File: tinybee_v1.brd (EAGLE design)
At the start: 47.6 x 27.8 mm, 22 parts, among them U1 ATTINY85-20S

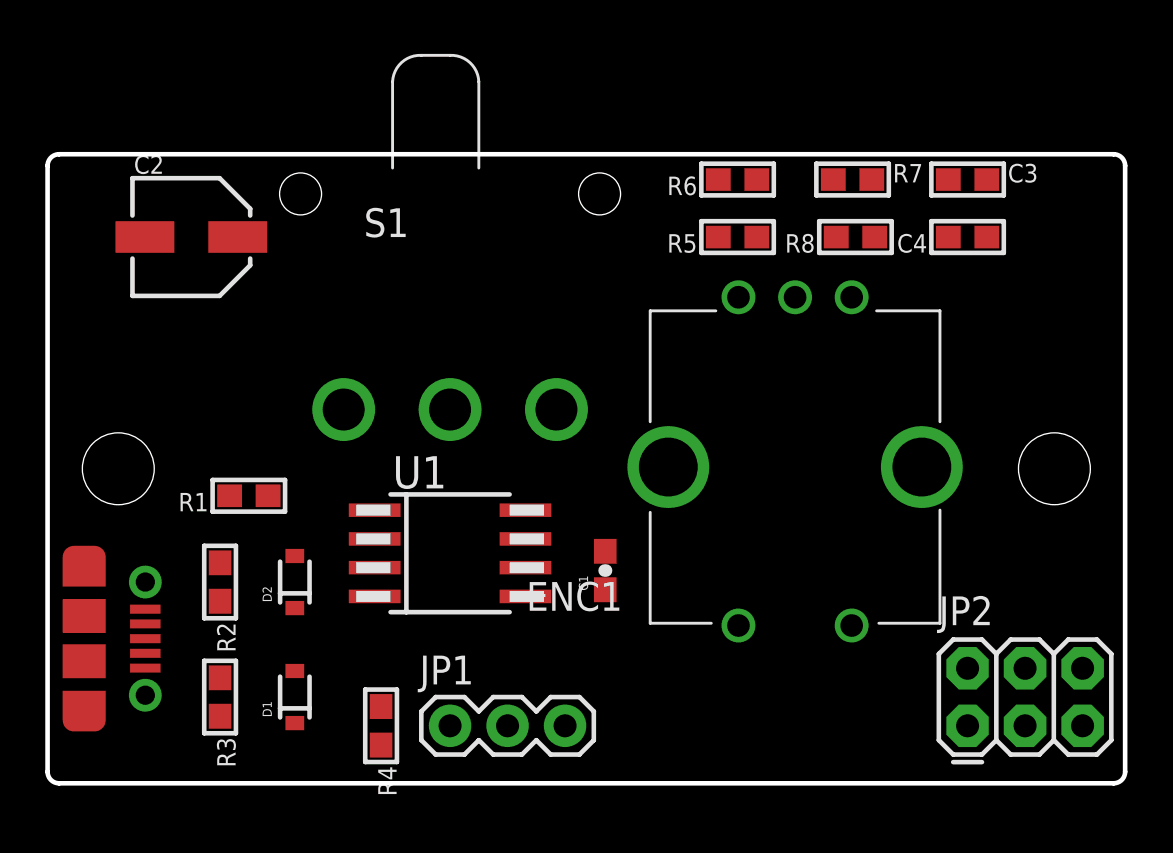
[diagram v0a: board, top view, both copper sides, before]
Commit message: Fixes after Eran review
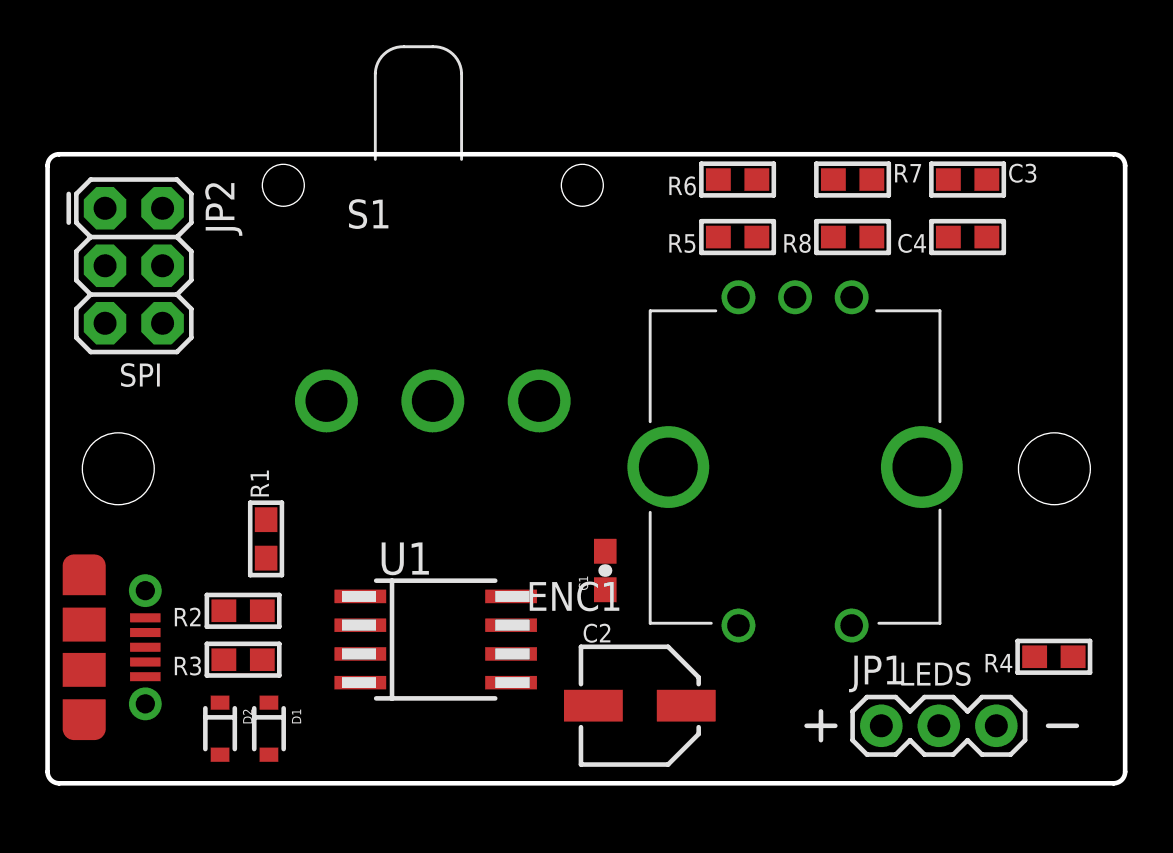
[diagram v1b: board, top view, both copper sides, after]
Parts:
- moved JP2 44.4 mm to (2.54, 25.4), turned to 270 degrees
- moved R4 29.9 mm to (44.5, 5.59), turned to 180 degrees
- moved C2 28.7 mm to (26.2, 3.43)
- moved JP1 19.0 mm to (36.8, 2.54)
- moved D2 7.27 mm to (7.62, 2.41), turned to 270 degrees
- moved U1 3.86 mm to (17.1, 6.35)
- moved R1 2.05 mm to (9.65, 10.8), turned to 90 degrees
- moved R3 1.94 mm to (8.64, 5.46), turned to 180 degrees
- moved D1 1.81 mm to (9.78, 2.41), turned to 270 degrees
- moved R2 1.63 mm to (8.64, 7.62), turned to 180 degrees
- moved S1 0.85 mm to (17.0, 16.9)
- moved USB 0.38 mm to (4.32, 8.51)
- moved R8 0.13 mm to (35.6, 24.1)
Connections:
- net N$1 renamed VBUS
- removed net N$5: C1.1, U1.8
- net GND: now also C1.2
- net VCC: now also C1.1, U1.8; no longer C1.2
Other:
- board text added: "LEDS"
- board text added: "SPI"

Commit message: moved a few pieces
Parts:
- moved ENC1 1.27 mm to (34.3, 14.0)
- moved C2 0.65 mm to (25.5, 3.56)
- moved C3 0.25 mm to (40.6, 26.4), turned to 180 degrees
- moved R6 0.25 mm to (30.5, 26.4)
- moved R7 0.25 mm to (35.6, 26.4)
- turned R8 to 0 degrees
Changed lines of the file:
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@@
 <attribute name="PROD_ID" value="CAP-00810" x="24.638" y="9.398" size="1.778" layer="27" rot="R90" display="off"/>
 </element>
-<element name="C2" library="microbuilder" package="PANASONIC_C" value="47uF" x="26.162" y="3.429"/>
-<element name="C3" library="microbuilder" package="0603" value="0.1uF" x="40.64" y="26.67"/>
+<element name="C2" library="microbuilder" package="PANASONIC_C" value="47uF" x="25.527" y="3.556"/>
+<element name="C3" library="microbuilder" package="0603" value="0.1uF" x="40.64" y="26.416" rot="R180"/>
 <element name="C4" library="microbuilder" package="0603" value="0.1uF" x="40.64" y="24.13" rot="R180"/>
 <element name="D1" library="SparkFun-DiscreteSemi" package="SOD-323" value="3.6V" x="9.779" y="2.413" rot="R270">
@@
 <element name="JP1" library="SparkFun-Connectors" package="1X03" value="LEDS" x="36.83" y="2.54"/>
 <element name="R5" library="microbuilder" package="0603" value="10k" x="30.48" y="24.13" rot="R180"/>
-<element name="R6" library="microbuilder" package="0603" value="10k" x="30.48" y="26.67" rot="R180"/>
-<element name="R7" library="microbuilder" package="0603" value="10k" x="35.56" y="26.67"/>
-<element name="R8" library="microbuilder" package="0603" value="10k" x="35.56" y="24.13" rot="R180"/>
+<element name="R6" library="microbuilder" package="0603" value="10k" x="30.48" y="26.416" rot="R180"/>
+<element name="R7" library="microbuilder" package="0603" value="10k" x="35.56" y="26.416"/>
+<element name="R8" library="microbuilder" package="0603" value="10k" x="35.56" y="24.13"/>
 <element name="U1" library="_hhn_attiny25_45_85" package="SOIC8_EIAJ_208MIL" value="ATTINY85-20S" x="17.145" y="6.35" rot="R270"/>
 <element name="USB" library="GeekAmmo" package="USB-MICRO-MOLEX-105017-0001" value="USB-CON-5PIN-105017-0001" x="4.318" y="8.509" rot="R270"/>
@@
 <element name="R2" library="microbuilder" package="0603" value="68R" x="8.636" y="7.62" rot="R180"/>
 <element name="R4" library="microbuilder" package="0603" value="220R" x="44.45" y="5.588" rot="R180"/>
-<element name="ENC1" library="Custom" package="ROTARY-ENCODER-PEC12R" value="" x="33.02" y="13.97" rot="R180"/>
+<element name="ENC1" library="Custom" package="ROTARY-ENCODER-PEC12R" value="" x="34.29" y="13.97" rot="R180"/>
 <element name="U$1" library="Custom" package="FB-30" value="" x="0" y="0"/>
 <element name="S1" library="Custom" package="SWITCH-SPDT-RIGHTANGLE-500" value="" x="17.018" y="16.891"/>
@@
 <contactref element="U1" pad="8"/>
 <contactref element="C1" pad="1"/>
-<wire x1="34.71" y1="24.13" x2="36.41" y2="26.67" width="0" layer="19" extent="1-1"/>
-<wire x1="24.638" y1="8.548" x2="34.71" y2="24.13" width="0" layer="19" extent="1-1"/>
+<wire x1="36.41" y1="24.13" x2="36.41" y2="26.416" width="0" layer="19" extent="1-1"/>
+<wire x1="24.638" y1="8.548" x2="36.41" y2="24.13" width="0" layer="19" extent="1-1"/>
 <wire x1="20.475" y1="8.255" x2="24.638" y2="8.548" width="0" layer="19" extent="1-1"/>
-<wire x1="28.212" y1="3.429" x2="24.638" y2="8.548" width="0" layer="19" extent="1-1"/>
-<wire x1="36.83" y1="2.54" x2="28.212" y2="3.429" width="0" layer="19" extent="1-1"/>
+<wire x1="27.577" y1="3.556" x2="24.638" y2="8.548" width="0" layer="19" extent="1-1"/>
+<wire x1="36.83" y1="2.54" x2="27.577" y2="3.556" width="0" layer="19" extent="1-1"/>
 <wire x1="17.018" y1="16.891" x2="20.475" y2="8.255" width="0" layer="19" extent="1-1"/>
 <wire x1="9.652" y1="11.645" x2="17.018" y2="16.891" width="0" layer="19" extent="1-1"/>
@@
 <contactref element="ENC1" pad="C"/>
 <contactref element="C1" pad="2"/>
-<wire x1="41.49" y1="24.13" x2="39.79" y2="26.67" width="0" layer="19" extent="1-1"/>
-<wire x1="33.02" y1="21.47" x2="39.79" y2="26.67" width="0" layer="19" extent="1-1"/>
-<wire x1="24.638" y1="10.248" x2="33.02" y2="21.47" width="0" layer="19" extent="1-1"/>
-<wire x1="24.112" y1="3.429" x2="24.638" y2="10.248" width="0" layer="19" extent="1-1"/>
-<wire x1="13.815" y1="4.445" x2="24.112" y2="3.429" width="0" layer="19" extent="1-1"/>
+<wire x1="41.49" y1="24.13" x2="41.49" y2="26.416" width="0" layer="19" extent="1-1"/>
+<wire x1="34.29" y1="21.47" x2="41.49" y2="24.13" width="0" layer="19" extent="1-1"/>
+<wire x1="36.79" y1="6.97" x2="34.29" y2="21.47" width="0" layer="19" extent="1-1"/>
+<wire x1="41.91" y1="2.54" x2="36.79" y2="6.97" width="0" layer="19" extent="1-1"/>
+<wire x1="24.638" y1="10.248" x2="36.79" y2="6.97" width="0" layer="19" extent="1-1"/>
+<wire x1="23.477" y1="3.556" x2="24.638" y2="10.248" width="0" layer="19" extent="1-1"/>
+<wire x1="13.815" y1="4.445" x2="23.477" y2="3.556" width="0" layer="19" extent="1-1"/>
 <wire x1="9.779" y1="1.263" x2="13.815" y2="4.445" width="0" layer="19" extent="1-1"/>
 <wire x1="7.62" y1="1.263" x2="9.779" y2="1.263" width="0" layer="19" extent="1-1"/>
 <wire x1="4.318" y1="4.709" x2="7.62" y2="1.263" width="0" layer="19" extent="1-1"/>
-<wire x1="35.52" y1="6.97" x2="24.638" y2="10.248" width="0" layer="19" extent="1-1"/>
-<wire x1="41.91" y1="2.54" x2="35.52" y2="6.97" width="0" layer="19" extent="1-1"/>
 <wire x1="5.08" y1="20.32" x2="4.318" y2="4.709" width="0" layer="19" extent="1-1"/>
 </signal>
@@
 <contactref element="R2" pad="1"/>
 <contactref element="ENC1" pad="SW2"/>
-<wire x1="13.815" y1="6.985" x2="30.52" y2="6.97" width="0" layer="19" extent="1-1"/>
+<wire x1="13.815" y1="6.985" x2="31.79" y2="6.97" width="0" layer="19" extent="1-1"/>
 <wire x1="9.486" y1="7.62" x2="13.815" y2="6.985" width="0" layer="19" extent="1-1"/>
 </signal>
@@
 <contactref element="R7" pad="1"/>
 <contactref element="ENC1" pad="A"/>
-<wire x1="31.33" y1="26.67" x2="34.71" y2="26.67" width="0" layer="19" extent="1-1"/>
-<wire x1="35.52" y1="21.47" x2="34.71" y2="26.67" width="0" layer="19" extent="1-1"/>
+<wire x1="31.33" y1="26.416" x2="34.71" y2="26.416" width="0" layer="19" extent="1-1"/>
+<wire x1="36.79" y1="21.47" x2="34.71" y2="26.416" width="0" layer="19" extent="1-1"/>
 </signal>
 <signal name="N$8">
@@
 <contactref element="R8" pad="1"/>
 <contactref element="ENC1" pad="B"/>
-<wire x1="31.33" y1="24.13" x2="36.41" y2="24.13" width="0" layer="19" extent="1-1"/>
-<wire x1="30.52" y1="21.47" x2="31.33" y2="24.13" width="0" layer="19" extent="1-1"/>
+<wire x1="31.33" y1="24.13" x2="34.71" y2="24.13" width="0" layer="19" extent="1-1"/>
+<wire x1="31.79" y1="21.47" x2="31.33" y2="24.13" width="0" layer="19" extent="1-1"/>
 </signal>
 <signal name="N$11">
@@
 <contactref element="C3" pad="2"/>
 <contactref element="JP2" pad="4"/>
-<wire x1="29.63" y1="26.67" x2="41.49" y2="26.67" width="0" layer="19" extent="1-1"/>
-<wire x1="20.475" y1="4.445" x2="29.63" y2="26.67" width="0" layer="19" extent="1-1"/>
+<wire x1="29.63" y1="26.416" x2="39.79" y2="26.416" width="0" layer="19" extent="1-1"/>
+<wire x1="20.475" y1="4.445" x2="29.63" y2="26.416" width="0" layer="19" extent="1-1"/>
 <wire x1="5.08" y1="22.86" x2="20.475" y2="4.445" width="0" layer="19" extent="1-1"/>
 </signal>

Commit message: route
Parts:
- removed FRAME1: FRAME-LETTER, SparkFun-Aesthetics:CREATIVE_COMMONS
- moved C4 11.8 mm to (29.0, 25.7)
- moved D2 7.87 mm to (7.62, 10.3), turned to 90 degrees
- moved R6 7.79 mm to (37.8, 23.9)
- moved R8 6.91 mm to (29.0, 22.1), turned to 180 degrees
- moved R4 6.12 mm to (38.4, 5.08), turned to 0 degrees
- moved R7 5.93 mm to (39.6, 22.1)
- moved C2 5.34 mm to (30.9, 3.30)
- moved C1 3.31 mm to (21.3, 9.65), turned to 0 degrees
- moved C3 2.90 mm to (37.8, 25.7)
- moved D1 2.09 mm to (7.75, 2.92)
- moved JP2 1.70 mm to (3.30, 23.9)
- moved R5 1.55 mm to (29.0, 23.9)
- moved R1 0.57 mm to (9.40, 10.3)
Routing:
- net PB0: track 0.00 -> 59.7 mm, vias 0 -> 2
- net PB1: track 0.00 -> 57.9 mm, vias 0 -> 2
- net PB2: track 0.00 -> 54.7 mm
- net VCC: track 0.00 -> 29.1 mm, vias 0 -> 4
- net PB3: track 0.00 -> 27.3 mm, vias 0 -> 1
- net VBUS: track 0.00 -> 17.5 mm, vias 0 -> 3
- net PB5: track 0.00 -> 15.6 mm
- net N$2: track 0.00 -> 7.35 mm
- net N$3: track 0.00 -> 5.10 mm
- net PB4: track 0.00 -> 4.43 mm
- net N$4: track 0.00 -> 4.05 mm
- net N$8: track 0.00 -> 4.02 mm
- net N$11: track 0.00 -> 2.61 mm
- added copper zone on layer 1, net GND
- added copper zone on layer 16, net VCC
